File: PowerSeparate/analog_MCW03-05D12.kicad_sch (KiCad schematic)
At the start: 15 parts, among them J1 RemoteOnOff, J2 A_Power, J3 A_Power, J7 A_Power, U1 Opamp_Dual

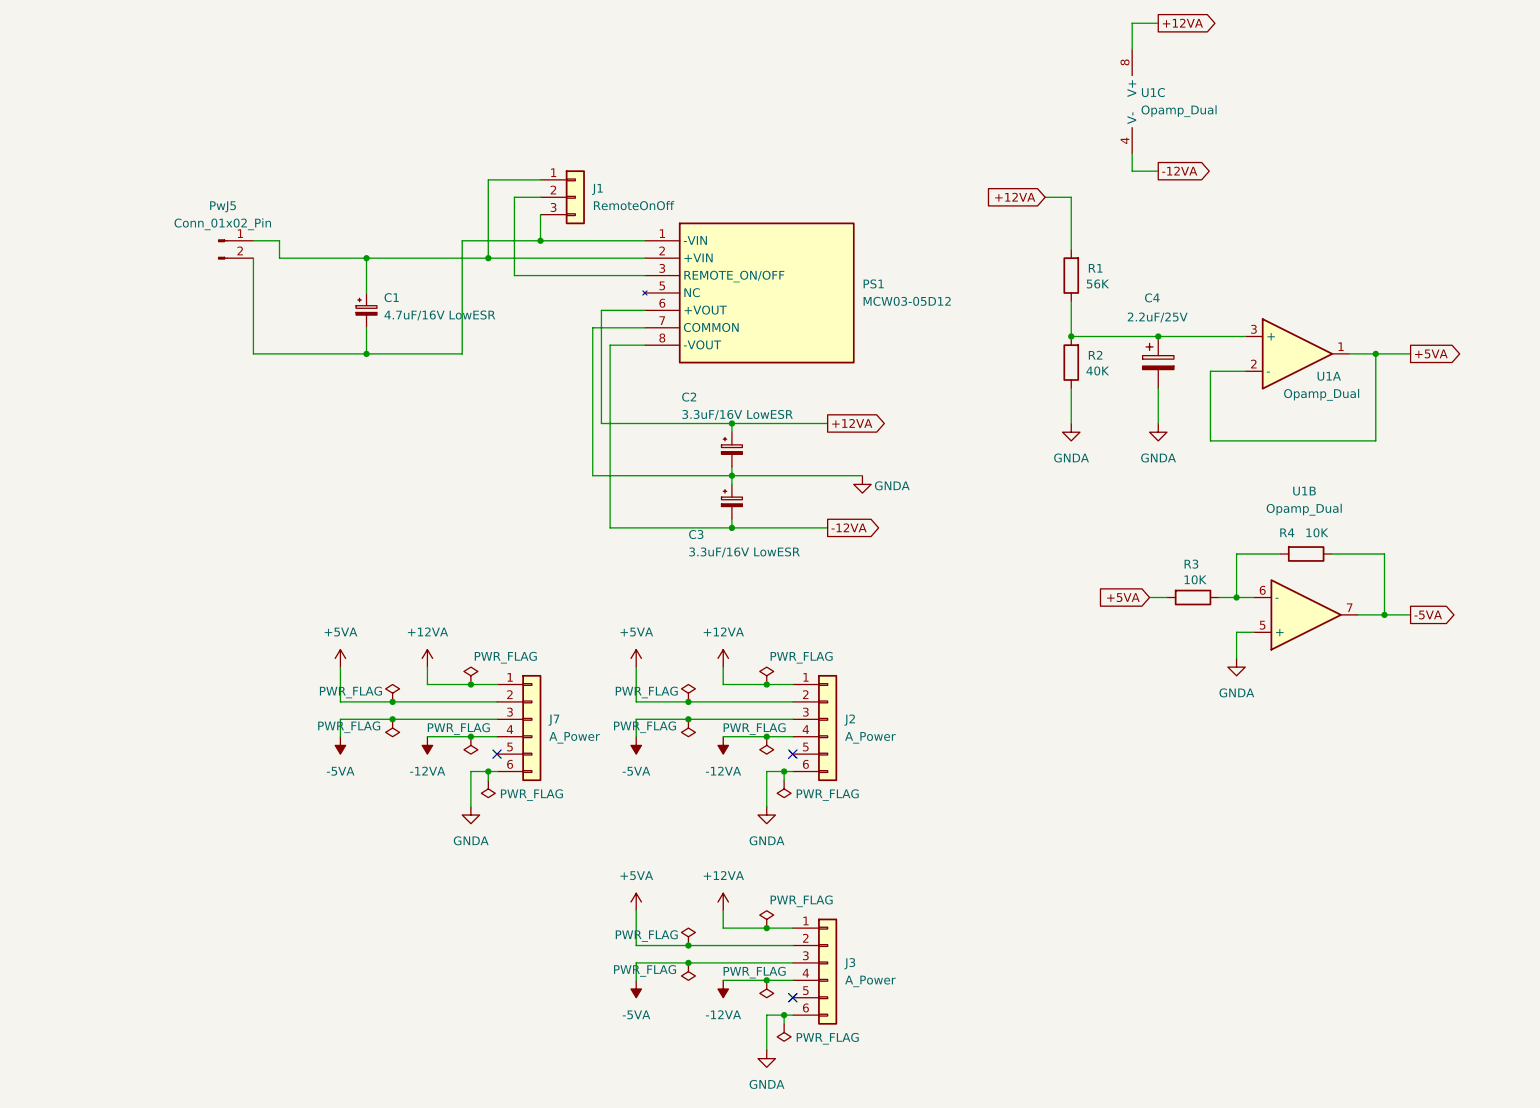
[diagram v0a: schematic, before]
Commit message: MC2
ガーバーデータ出力
BOMファイル出力
NJM2374A関連プロジェクトを作成
PowerSeparateが完了
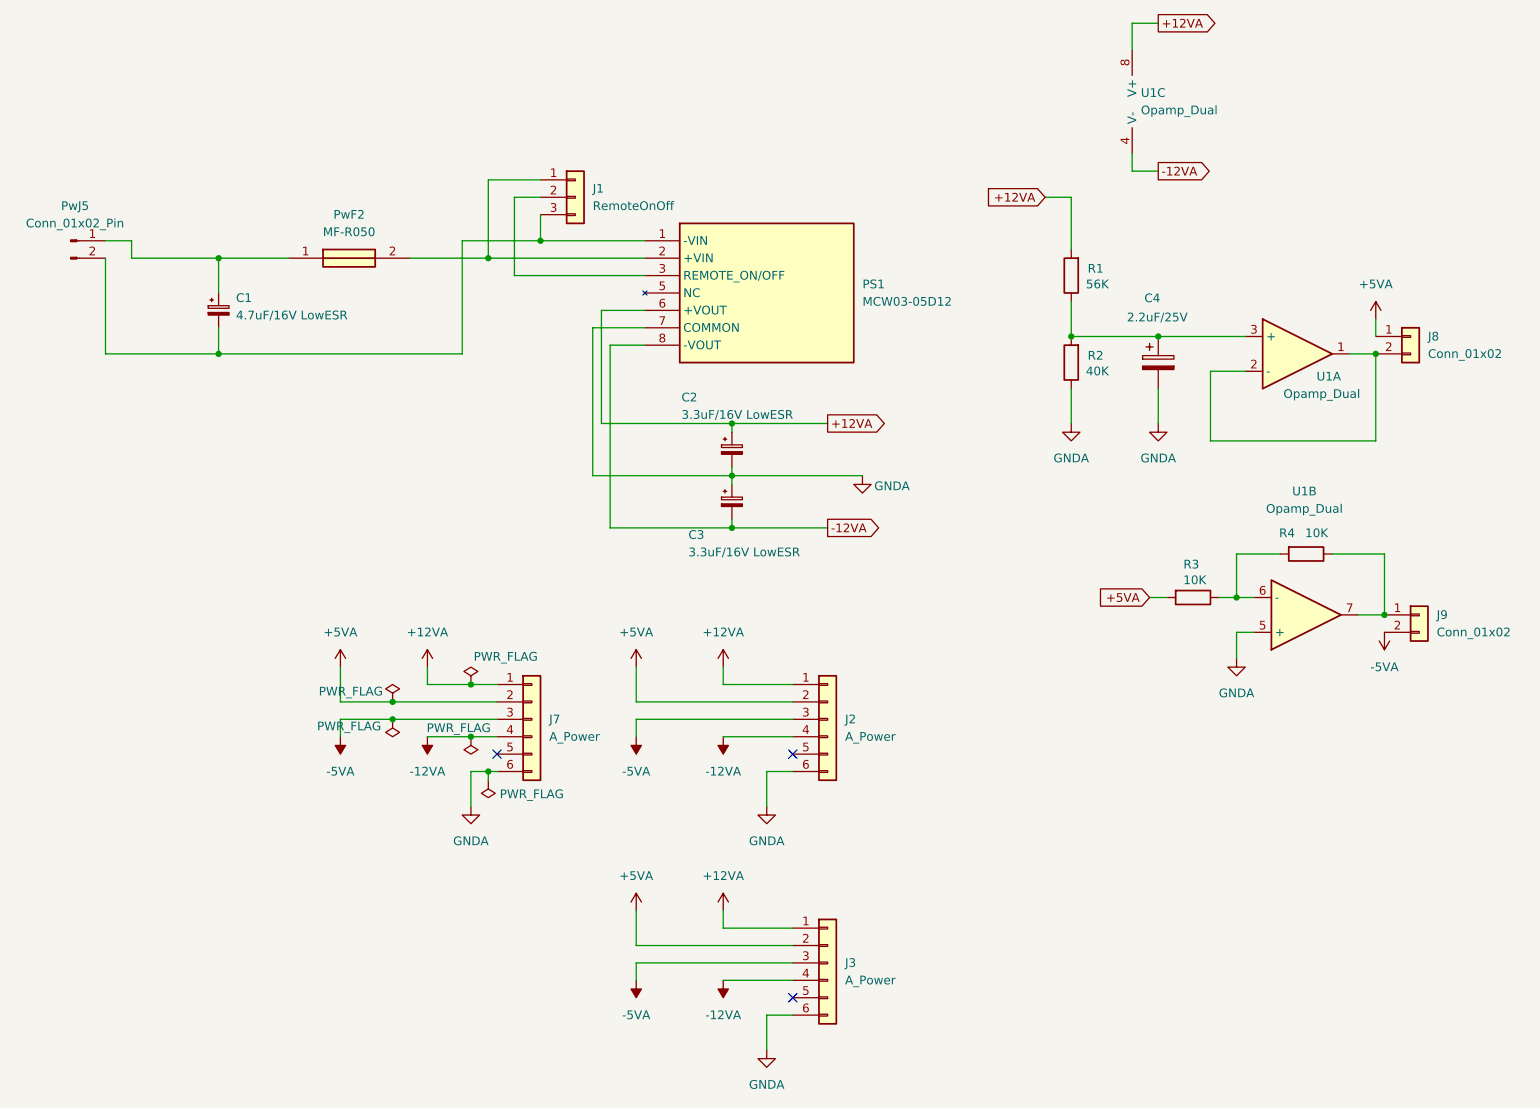
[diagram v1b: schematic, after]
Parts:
- added J8, J9: Conn_01x02, Connector_PinHeader_2.54mm:PinHeader_1x02_P2.54mm_Vertical, symbol Connector_Generic:Conn_01x02
- added PwF2: MF-R050, SamacSys_Parts:MFR050, symbol SamacSys_Parts:MF-R050
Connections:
- net +5VA: now also J8.1 (Pin_1); no longer U1.1, U1.2 (-)
- net -5VA: now also J9.2 (Pin_2); no longer R4.1, U1.7
- net at C1.1, PwJ5.1 (Pin_1): now also PwF2.1; no longer J1.1 (Pin_1), PS1.2 (+VIN)
- new net: J8.2 (Pin_2), U1.1, U1.2 (-)
- new net: J1.1 (Pin_1), PS1.2 (+VIN), PwF2.2
- new net: J9.1 (Pin_1), R4.1, U1.7
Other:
- moved on the sheet: C1, PwJ5
